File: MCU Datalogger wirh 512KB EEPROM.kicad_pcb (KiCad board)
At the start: 2 copper layers, 29 parts, among them IC1 ATMEGA328P-AU, J1 Conn_01x04_Pin, J2 Conn_01x04_Pin, J3 Conn_01x09_Pin, J4 Conn_02x03_Odd_Even, U1 24LC1025, U2 24LC1025, U3 DS1137S+, Y1 16 MHz, Y2 32.768 KHz

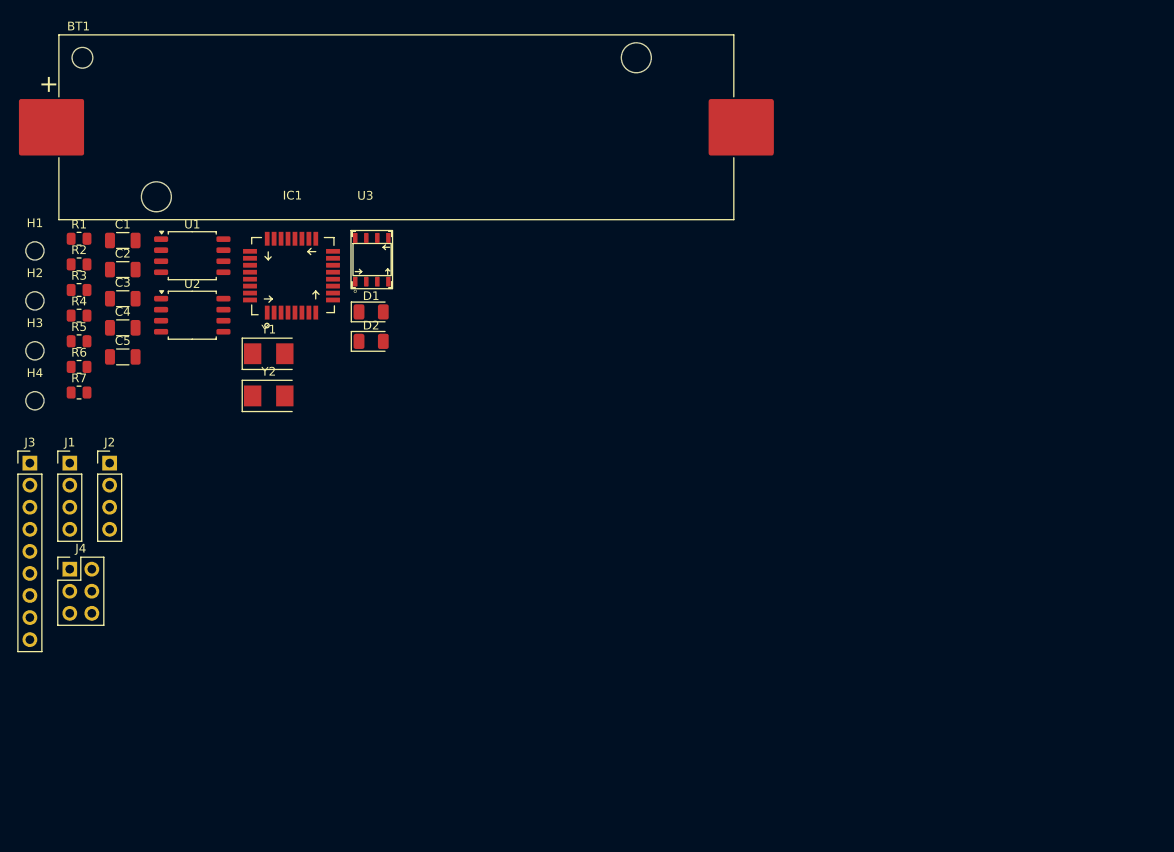
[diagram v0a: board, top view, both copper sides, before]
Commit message: Done the layout and wiring of the 2 layered PCB.
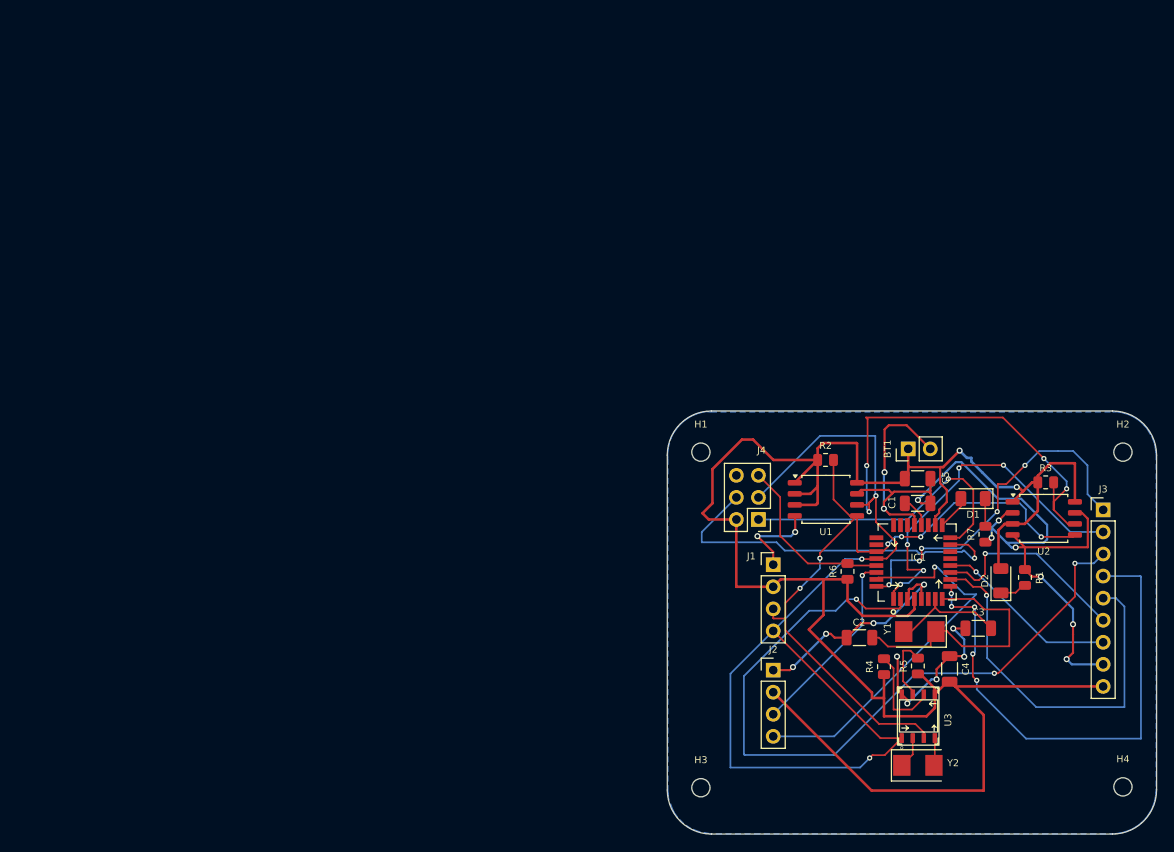
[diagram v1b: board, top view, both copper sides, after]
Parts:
- BT1: footprint Battery:BatteryHolder_Keystone_1042_1x18650 -> Connector_PinHeader_2.54mm:PinHeader_1x02_P2.54mm_Vertical
- moved H4 132.9 mm to (160.2, 118.0)
- moved H2 126.4 mm to (160.2, 79.5)
- moved J3 123.6 mm to (157.9, 86.1)
- moved R1 115.6 mm to (148.9, 93.9), turned to 90 degrees
- moved R3 113.4 mm to (151.3, 82.9)
- moved R7 105.6 mm to (144.3, 88.9), turned to 90 degrees
- moved C3 105.5 mm to (143.5, 99.7)
- moved R5 103.5 mm to (136.6, 104.1), turned to 90 degrees
- moved C4 102.9 mm to (140.2, 104.4), turned to -90 degrees
- moved R4 101.1 mm to (132.7, 104.1), turned to 90 degrees
- moved U2 100.8 mm to (151.1, 87.1)
- moved C1 96.4 mm to (136.6, 85.3)
- moved C2 94.8 mm to (129.8, 100.8)
- moved C5 92.6 mm to (136.6, 82.5)
- moved H3 91.7 mm to (111.6, 118.1)
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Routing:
- net /Vcc: track 0.00 -> 241.6 mm, vias 0 -> 2
- net GND: track 0.00 -> 165.1 mm, vias 0 -> 20
- net /SCL: track 0.00 -> 159.4 mm, vias 0 -> 7
- net /D4: track 0.00 -> 85.4 mm, vias 0 -> 3
- net /SDA: track 0.00 -> 82.9 mm, vias 0 -> 6
- net /D5: track 0.00 -> 59.4 mm, vias 0 -> 5
- net /D6: track 0.00 -> 45.0 mm, vias 0 -> 1
- net /TX: track 0.00 -> 44.4 mm, vias 0 -> 1
- net /MOSI: track 0.00 -> 43.2 mm, vias 0 -> 1
- net /D2: track 0.00 -> 41.4 mm, vias 0 -> 5
- net /D3: track 0.00 -> 41.3 mm, vias 0 -> 5
- net /MISO: track 0.00 -> 34.4 mm, vias 0 -> 1
- net Net-(IC1-PB7): track 0.00 -> 31.7 mm
- net /D7: track 0.00 -> 23.8 mm, vias 0 -> 1
- net /RX: track 0.00 -> 22.0 mm, vias 0 -> 1
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- added copper zone on B.Cu, net GND
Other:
- board outline added: 56.3 x 48.7 mm

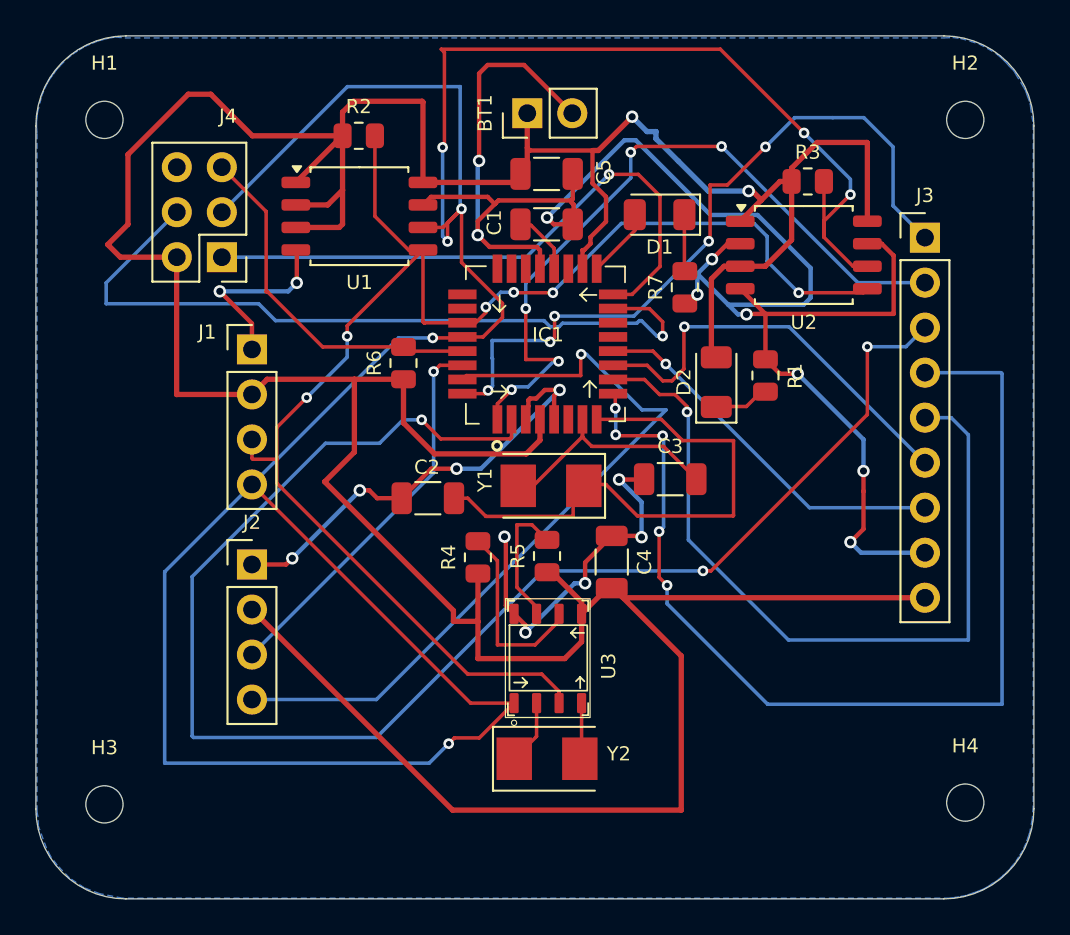
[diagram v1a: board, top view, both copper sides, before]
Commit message: Added graphics at the back silkscreen and also on the front silkscreen for connector pins.
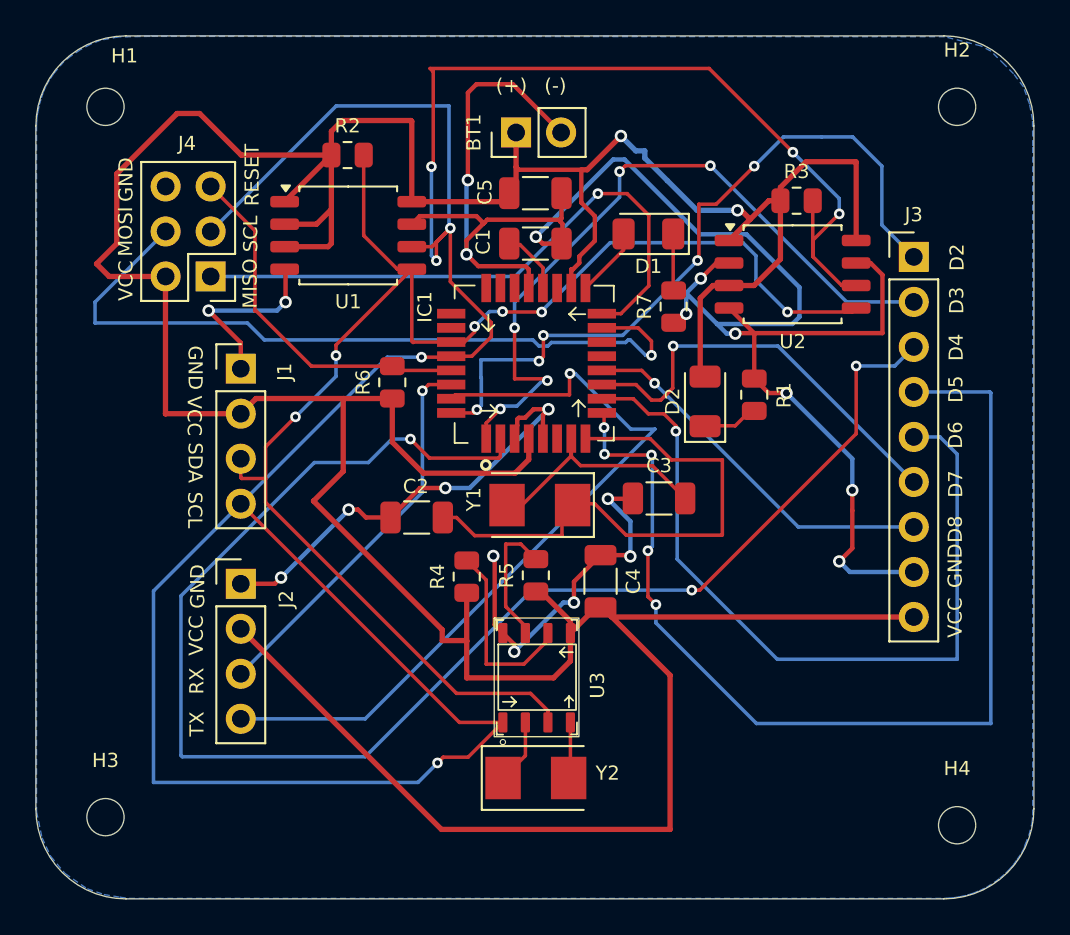
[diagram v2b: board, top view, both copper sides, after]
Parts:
- added REF**: KiCad-Logo2_8mm_SilkScreen, Symbol:KiCad-Logo2_8mm_SilkScreen, B.Cu at (144.1, 116.3)
- moved H4 1.36 mm to (159.7, 119.3)
- moved C3 1.26 mm to (142.9, 100.8)
- moved C5 1.26 mm to (135.9, 83.6)
- moved D1 1.26 mm to (142.3, 85.9)
- moved IC1 1.26 mm to (133.1, 97.4)
- moved J3 1.26 mm to (157.3, 87.2)
- moved R1 1.26 mm to (148.3, 95.0)
- moved U3 1.26 mm to (134.1, 113.4)
- moved Y1 1.26 mm to (136.2, 101.2)
- moved R2 1.26 mm to (125.3, 81.4)
- moved BT1 1.26 mm to (134.8, 80.2)
- moved R4 1.26 mm to (132.0, 105.2)
- moved C1 1.26 mm to (135.9, 86.4)
- moved C2 1.26 mm to (129.2, 101.9)
- moved D2 1.26 mm to (145.5, 95.3)
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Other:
- board text added: "(+)"
- board text added: "(-)"
- board text added: "D2"
- board text added: "D3"
- board text added: "D4"
- board text added: "D5"
- board text added: "D6"
- board text added: "D7"
- board text added: "D8"
- board text added: "GND"
- board text added: "MISO"
- board text added: "MOSI"
- board text added: "RESET"
- board text added: "RX"
- board text added: "SCL"
- board text added: "SDA"
- board text added: "TX"
- board text added: "VCC"

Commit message: Improved some tracks.
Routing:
- net /Vcc: track 241.6 -> 237.2 mm
- net /SCL: track 159.4 -> 157.8 mm
- net /MOSI: track 43.2 -> 41.7 mm
- net /D6: track 45.0 -> 46.0 mm
- net /D5: track 59.4 -> 58.6 mm
- net GND: track 165.1 -> 164.6 mm
- net /D4: track 85.4 -> 84.9 mm
